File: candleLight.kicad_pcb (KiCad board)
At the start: 2 copper layers, 37.7 x 22.8 mm, 35 parts, among them P501 USB_OTG, U201 STM32F072C8Tx, U301 MCP1754ST-3302E/MB, U401 TJA1051/3, X501 CON_SWD, X502 SUB-D9, Y201 8MHz

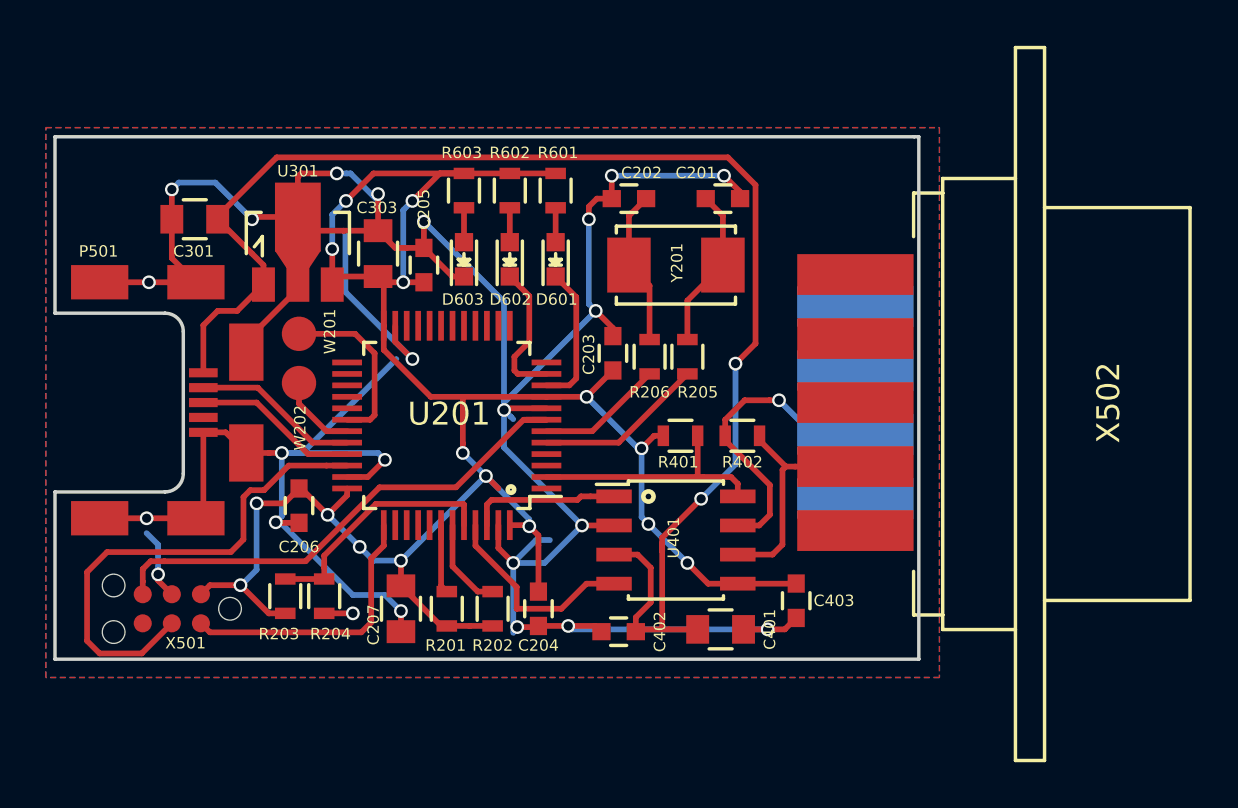
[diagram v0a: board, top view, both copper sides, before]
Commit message: set subd9 pin 3 to gnd, correct solder mask margin
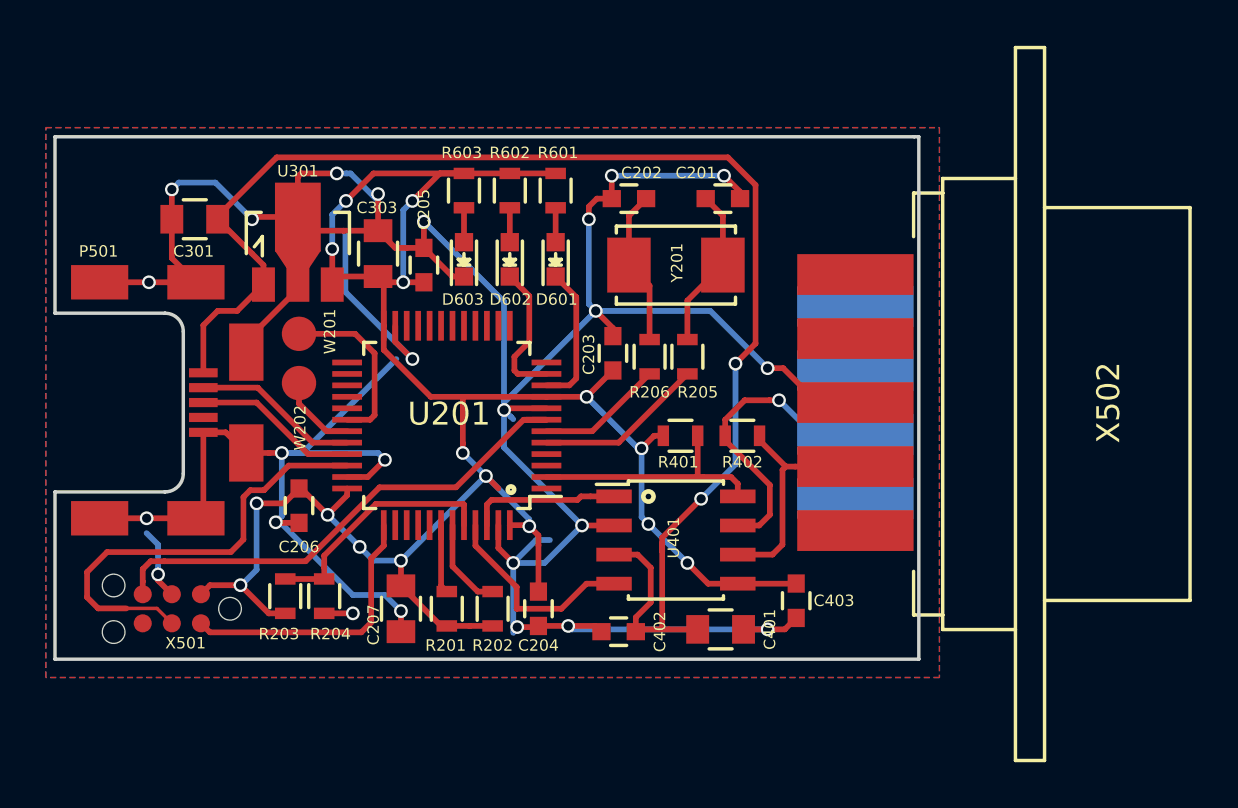
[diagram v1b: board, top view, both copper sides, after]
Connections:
- X502 pad 3: Net-(X502-Pad3) -> GND
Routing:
- net GND: track 157.4 -> 170.4 mm, vias 24 -> 25
- net /Connectors/SWDIO: track 21.8 -> 19.6 mm
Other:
- rule pad_to_mask_clearance: 0.2 -> 0.05
- rule trace_min: 0.2 -> 0.15
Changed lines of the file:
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@@
 (kicad_pcb (version 4) (host pcbnew 4.0.2-4+6225~38~ubuntu15.10.1-stable)
   (general
-    (links 85)
+    (links 86)
     (no_connects 0)
     (area 41.324999 73.324999 79.175001 96.275001)
     (thickness 1.6)
     (drawings 15)
-    (tracks 376)
+    (tracks 382)
     (zones 0)
     (modules 35)
-    (nets 59)
+    (nets 58)
   )
   (page A4)
@@
     (37 F.SilkS user)
     (38 B.Mask user)
-    (39 F.Mask user hide)
+    (39 F.Mask user)
     (40 Dwgs.User user)
     (41 Cmts.User user)
@@
   (setup
     (last_trace_width 0.25)
+    (user_trace_width 0.15)
     (trace_clearance 0.15)
     (zone_clearance 0.2)
     (zone_45_only no)
-    (trace_min 0.2)
-    (segment_width 0.2)
+    (trace_min 0.15)
+    (segment_width 0.1)
     (edge_width 0.15)
     (via_size 0.6)
@@
     (pad_size 1.524 1.524)
     (pad_drill 0.762)
-    (pad_to_mask_clearance 0.2)
-    (aux_axis_origin 0 0)
+    (pad_to_mask_clearance 0.05)
+    (aux_axis_origin 41.5 73.5)
+    (grid_origin 41.5 73.5)
     (visible_elements FFFFFF7F)
     (pcbplotparams
-      (layerselection 0x00030_80000001)
-      (usegerberextensions false)
+      (layerselection 0x010c0_80000001)
+      (usegerberextensions true)
       (excludeedgelayer true)
       (linewidth 0.100000)
@@
       (drillshape 0)
       (scaleselection 1)
-      (outputdirectory ""))
+      (outputdirectory gerber/))
   )
   (net 0 "")
@@
   (net 49 /MCU/CAN_TX)
   (net 50 "Net-(X501-Pad6)")
-  (net 51 "Net-(X502-Pad3)")
-  (net 52 "Net-(X502-Pad4)")
-  (net 53 "Net-(X502-Pad5)")
-  (net 54 "Net-(X502-Pad1)")
-  (net 55 "Net-(X502-Pad9)")
-  (net 56 "Net-(X502-Pad8)")
-  (net 57 "Net-(X502-Pad6)")
-  (net 58 "Net-(U201-Pad41)")
+  (net 51 "Net-(X502-Pad4)")
+  (net 52 "Net-(X502-Pad5)")
+  (net 53 "Net-(X502-Pad1)")
+  (net 54 "Net-(X502-Pad9)")
+  (net 55 "Net-(X502-Pad8)")
+  (net 56 "Net-(X502-Pad6)")
+  (net 57 "Net-(U201-Pad41)")
   (net_class Default "This is the default net class."
     (clearance 0.15)
@@
     (add_net "Net-(X501-Pad6)")
     (add_net "Net-(X502-Pad1)")
-    (add_net "Net-(X502-Pad3)")
     (add_net "Net-(X502-Pad4)")
     (add_net "Net-(X502-Pad5)")
@@
       (net 47 "Net-(U201-Pad40)"))
     (pad 41 smd rect (at 0.75 -4.35 270) (size 1.3 0.25) (layers F.Cu F.Paste F.Mask)
-      (net 58 "Net-(U201-Pad41)"))
+      (net 57 "Net-(U201-Pad41)"))
     (pad 42 smd rect (at 0.25 -4.35 270) (size 1.3 0.25) (layers F.Cu F.Paste F.Mask)
       (net 14 "Net-(R201-Pad2)"))
@@
       (net 21 /CAN/CAN_L))
     (pad 3 connect rect (at 0 2.667 270) (size 1.778 5.08) (layers F.Cu F.Mask)
-      (net 51 "Net-(X502-Pad3)"))
+      (net 1 GND))
     (pad 4 connect rect (at -2.794 2.667 270) (size 1.778 5.08) (layers F.Cu F.Mask)
-      (net 52 "Net-(X502-Pad4)"))
+      (net 51 "Net-(X502-Pad4)"))
     (pad 5 connect rect (at -5.588 2.667 270) (size 1.778 5.08) (layers F.Cu F.Mask)
-      (net 53 "Net-(X502-Pad5)"))
+      (net 52 "Net-(X502-Pad5)"))
     (pad 1 connect rect (at 5.588 2.667 270) (size 1.778 5.08) (layers F.Cu F.Mask)
-      (net 54 "Net-(X502-Pad1)"))
+      (net 53 "Net-(X502-Pad1)"))
     (pad 9 connect rect (at -4.191 2.667 270) (size 1.778 5.08) (layers B.Cu B.Mask)
-      (net 55 "Net-(X502-Pad9)"))
+      (net 54 "Net-(X502-Pad9)"))
     (pad 8 connect rect (at -1.397 2.667 270) (size 1.778 5.08) (layers B.Cu B.Mask)
-      (net 56 "Net-(X502-Pad8)"))
+      (net 55 "Net-(X502-Pad8)"))
     (pad 7 connect rect (at 1.397 2.667 270) (size 1.778 5.08) (layers B.Cu B.Mask)
       (net 20 /CAN/CAN_H))
     (pad 6 connect rect (at 4.191 2.667 270) (size 1.778 5.08) (layers B.Cu B.Mask)
-      (net 57 "Net-(X502-Pad6)"))
+      (net 56 "Net-(X502-Pad6)"))
     (model Connect.3dshapes/DB9M_CI.wrl
       (at (xyz 0 0 -0.033))
@@
   (gr_line (start 78.9 73.4) (end 79.1 73.4) (angle 90) (layer Edge.Cuts) (width 0.15))
   (gr_line (start 41.4 73.4) (end 78.9 73.4) (angle 90) (layer Edge.Cuts) (width 0.15))
+  (segment (start 72.5 83.5) (end 70 81) (width 0.25) (layer B.Cu) (net 1))
+  (segment (start 70 81) (end 65 81) (width 0.25) (layer B.Cu) (net 1))
+  (segment (start 76.333 85) (end 74.682 85) (width 0.25) (layer F.Cu) (net 1))
+  (via (at 72.5 83.5) (size 0.6) (drill 0.4) (layers F.Cu B.Cu) (net 1))
+  (segment (start 74.682 85) (end 73.182 83.5) (width 0.25) (layer F.Cu) (net 1))
+  (segment (start 73.182 83.5) (end 72.5 83.5) (width 0.25) (layer F.Cu) (net 1))
   (segment (start 54.124264 75) (end 53.7 75) (width 0.25) (layer B.Cu) (net 1))
   (segment (start 54.3 75) (end 54.124264 75) (width 0.25) (layer B.Cu) (net 1))
@@
   (segment (start 52.05 85.05) (end 52.05 84.15) (width 0.25) (layer F.Cu) (net 42))
   (segment (start 53.25 86.25) (end 52.05 85.05) (width 0.25) (layer F.Cu) (net 42))
-  (segment (start 46.5 94.635) (end 45.185 95.95) (width 0.25) (layer F.Cu) (net 43))
-  (segment (start 53.25 87.75) (end 54.15 87.75) (width 0.25) (layer F.Cu) (net 43))
-  (segment (start 45.185 95.95) (end 43.35 95.95) (width 0.25) (layer F.Cu) (net 43))
-  (segment (start 43.35 95.95) (end 42.8 95.4) (width 0.25) (layer F.Cu) (net 43))
-  (segment (start 42.8 95.4) (end 42.8 92.4) (width 0.25) (layer F.Cu) (net 43))
-  (segment (start 51.598996 87.75) (end 53.25 87.75) (width 0.25) (layer F.Cu) (net 43))
-  (segment (start 42.8 92.4) (end 43.675013 91.524987) (width 0.25) (layer F.Cu) (net 43))
-  (segment (start 43.675013 91.524987) (end 49.075013 91.524987) (width 0.25) (layer F.Cu) (net 43))
-  (segment (start 49.075013 91.524987) (end 49.624998 90.975002) (width 0.25) (layer F.Cu) (net 43))
-  (segment (start 49.624998 90.975002) (end 49.624998 89.123998) (width 0.25) (layer F.Cu) (net 43))
-  (segment (start 49.923998 88.824998) (end 50.523998 88.824998) (width 0.25) (layer F.Cu) (net 43))
-  (segment (start 49.624998 89.123998) (end 49.923998 88.824998) (width 0.25) (layer F.Cu) (net 43))
-  (segment (start 50.523998 88.824998) (end 51.598996 87.75) (width 0.25) (layer F.Cu) (net 43))
+  (segment (start 54.15 87.75) (end 51.598996 87.75) (width 0.25) (layer F.Cu) (net 43))
+  (segment (start 49.624998 89.123998) (end 49.624998 90.975002) (width 0.25) (layer F.Cu) (net 43))
+  (segment (start 43.283701 93.983701) (end 44.516299 93.983701) (width 0.25) (layer F.Cu) (net 43))
+  (segment (start 51.598996 87.75) (end 50.523998 88.824998) (width 0.25) (layer F.Cu) (net 43))
+  (segment (start 49.624998 90.975002) (end 49.075013 91.524987) (width 0.25) (layer F.Cu) (net 43))
+  (segment (start 50.523998 88.824998) (end 49.923998 88.824998) (width 0.25) (layer F.Cu) (net 43))
+  (segment (start 49.923998 88.824998) (end 49.624998 89.123998) (width 0.25) (layer F.Cu) (net 43))
+  (segment (start 49.075013 91.524987) (end 43.675013 91.524987) (width 0.25) (layer F.Cu) (net 43))
+  (segment (start 43.675013 91.524987) (end 42.8 92.4) (width 0.25) (layer F.Cu) (net 43))
+  (segment (start 42.8 92.4) (end 42.8 93.5) (width 0.25) (layer F.Cu) (net 43))
+  (segment (start 42.8 93.5) (end 43.283701 93.983701) (width 0.25) (layer F.Cu) (net 43))
+  (segment (start 46.5 94.635) (end 45.848701 93.983701) (width 0.15) (layer F.Cu) (net 43))
+  (segment (start 45.848701 93.983701) (end 44.516299 93.983701) (width 0.15) (layer F.Cu) (net 43))
   (segment (start 47.77 94.635) (end 48.163699 95.028699) (width 0.25) (layer F.Cu) (net 44))
   (segment (start 48.163699 95.028699) (end 54.771301 95.028699) (width 0.25) (layer F.Cu) (net 44))

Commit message: add missing usb data line resistors
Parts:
- added R207: 22R, Resistors_SMD:R_0603, F.Cu at (52.1, 86.4)
- added R208: 22R, Resistors_SMD:R_0603, F.Cu at (52.1, 83.6)
- W201, W202: moved to B.Cu
- moved W201 5.78 mm to (56.6, 85.5)
- moved W202 2.75 mm to (54.5, 85.5)
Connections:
- U201 pad 32: /Connectors/USB_DM -> Net-(R208-Pad2)
- U201 pad 33: /Connectors/USB_DP -> Net-(R207-Pad1)
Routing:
- net GND: track 170.4 -> 166.1 mm
- net Net-(R208-Pad2): track 0.00 -> 3.89 mm
- net Net-(U201-Pad30): track 7.63 -> 4.61 mm, vias 0 -> 1
- net /Connectors/USB_DP: track 7.21 -> 4.49 mm
- net Net-(R207-Pad1): track 0.00 -> 2.37 mm
- net /Connectors/USB_DM: track 7.27 -> 5.14 mm
- net Net-(U201-Pad31): track 3.50 -> 3.22 mm, vias 0 -> 1

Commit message: add fiducials
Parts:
- added FID101: Dummy_FIDUCIAL_Passermarke_Type1_RevE_Date16Nov2011, Fiducials:Fiducial_1mm_Dia_2.54mm_Outer_CopperTop, F.Cu at (43.5, 75.5)
- added FID102: Dummy_FIDUCIAL_Passermarke_Type1_RevE_Date16Nov2011, Fiducials:Fiducial_1mm_Dia_2.54mm_Outer_CopperTop, F.Cu at (76.5, 93.5)
- added FID103: Dummy_FIDUCIAL_Passermarke_Type1_RevE_Date16Nov2011, Fiducials:Fiducial_1mm_Dia_2.54mm_Outer_CopperTop, F.Cu at (76.5, 75.5)
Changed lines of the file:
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@@
     (tracks 395)
     (zones 0)
-    (modules 37)
-    (nets 60)
+    (modules 40)
+    (nets 63)
   )
   (page A4)
@@
     (pad_drill 0.762)
     (pad_to_mask_clearance 0.05)
-    (aux_axis_origin 41.5 73.5)
+    (aux_axis_origin 43.5 75.5)
     (grid_origin 41.5 73.5)
     (visible_elements FFFFFF7F)
@@
   (net 58 "Net-(R207-Pad1)")
   (net 59 "Net-(R208-Pad2)")
+  (net 60 "Net-(FID101-Pad~)")
+  (net 61 "Net-(FID102-Pad~)")
+  (net 62 "Net-(FID103-Pad~)")
   (net_class Default "This is the default net class."
     (clearance 0.15)
@@
     (add_net "Net-(D602-Pad2)")
     (add_net "Net-(D603-Pad2)")
+    (add_net "Net-(FID101-Pad~)")
+    (add_net "Net-(FID102-Pad~)")
+    (add_net "Net-(FID103-Pad~)")
     (add_net "Net-(P501-Pad4)")
     (add_net "Net-(R201-Pad2)")
@@
     (tags "capacitor 0805")
     (attr smd)
-    (fp_text reference C401 (at 2.15 0 90) (layer F.SilkS)
+    (fp_text reference C401 (at -2.05 0.1 270) (layer F.SilkS)
       (effects (font (size 0.5 0.5) (thickness 0.125)))
     )
@@
     (tags "capacitor 0603")
     (attr smd)
-    (fp_text reference C402 (at -1.8 0 270) (layer F.SilkS)
+    (fp_text reference C402 (at 1.6 0 270) (layer F.SilkS)
       (effects (font (size 0.5 0.5) (thickness 0.125)))
     )
@@
     (tags "capacitor 0603")
     (attr smd)
-    (fp_text reference C403 (at 0 -1.65 360) (layer F.SilkS)
+    (fp_text reference C403 (at 1.95 -0.05 360) (layer F.SilkS)
       (effects (font (size 0.5 0.5) (thickness 0.125)))
     )
@@
       (net 42 "Net-(U201-Pad31)"))
   )
+  (module Fiducials:Fiducial_1mm_Dia_2.54mm_Outer_CopperTop (layer F.Cu)
+    (at 43.5 75.5)
+    (descr "Circular Fiducial, 1mm bare copper top; 2.54mm keepout")
+    (tags marker)
+    (attr virtual)
+    (fp_text reference FID101 (at 2.6 -1.1) (layer F.SilkS)
+      (effects (font (size 0.5 0.5) (thickness 0.125)))
+    )
+    (fp_text value Dummy_FIDUCIAL_Passermarke_Type1_RevE_Date16Nov2011 (at 0 -1.8) (layer F.Fab)
+      (effects (font (size 1 1) (thickness 0.15)))
+    )
+    (fp_circle (center 0 0) (end 1.55 0) (layer F.CrtYd) (width 0.05))
+    (pad ~ smd circle (at 0 0) (size 1 1) (layers F.Cu F.Mask)
+      (net 60 "Net-(FID101-Pad~)") (solder_mask_margin 0.77) (clearance 0.77))
+  )
+  (module Fiducials:Fiducial_1mm_Dia_2.54mm_Outer_CopperTop (layer F.Cu)
+    (at 76.5 93.5)
+    (descr "Circular Fiducial, 1mm bare copper top; 2.54mm keepout")
+    (tags marker)
+    (attr virtual)
+    (fp_text reference FID102 (at 0.9 2) (layer F.SilkS)
+      (effects (font (size 0.5 0.5) (thickness 0.125)))
+    )
+    (fp_text value Dummy_FIDUCIAL_Passermarke_Type1_RevE_Date16Nov2011 (at 0 -1.8) (layer F.Fab)
+      (effects (font (size 1 1) (thickness 0.15)))
+    )
+    (fp_circle (center 0 0) (end 1.55 0) (layer F.CrtYd) (width 0.05))
+    (pad ~ smd circle (at 0 0) (size 1 1) (layers F.Cu F.Mask)
+      (net 61 "Net-(FID102-Pad~)") (solder_mask_margin 0.77) (clearance 0.77))
+  )
+  (module Fiducials:Fiducial_1mm_Dia_2.54mm_Outer_CopperTop (layer F.Cu)
+    (at 76.5 75.5)
+    (descr "Circular Fiducial, 1mm bare copper top; 2.54mm keepout")
+    (tags marker)
+    (attr virtual)
+    (fp_text reference FID103 (at -2.7 -1.1) (layer F.SilkS)
+      (effects (font (size 0.5 0.5) (thickness 0.125)))
+    )
+    (fp_text value Dummy_FIDUCIAL_Passermarke_Type1_RevE_Date16Nov2011 (at 0 -1.8) (layer F.Fab)
+      (effects (font (size 1 1) (thickness 0.15)))
+    )
+    (fp_circle (center 0 0) (end 1.55 0) (layer F.CrtYd) (width 0.05))
+    (pad ~ smd circle (at 0 0) (size 1 1) (layers F.Cu F.Mask)
+      (net 62 "Net-(FID103-Pad~)") (solder_mask_margin 0.77) (clearance 0.77))
+  )
   (gr_circle (center 67.3 89.1) (end 67.5 89.2) (layer F.SilkS) (width 0.2))
